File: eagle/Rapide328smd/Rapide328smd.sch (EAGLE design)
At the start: 34 parts, among them IC1 MEGA8-AI, J1 AVR_SPI_PRG_6PTH

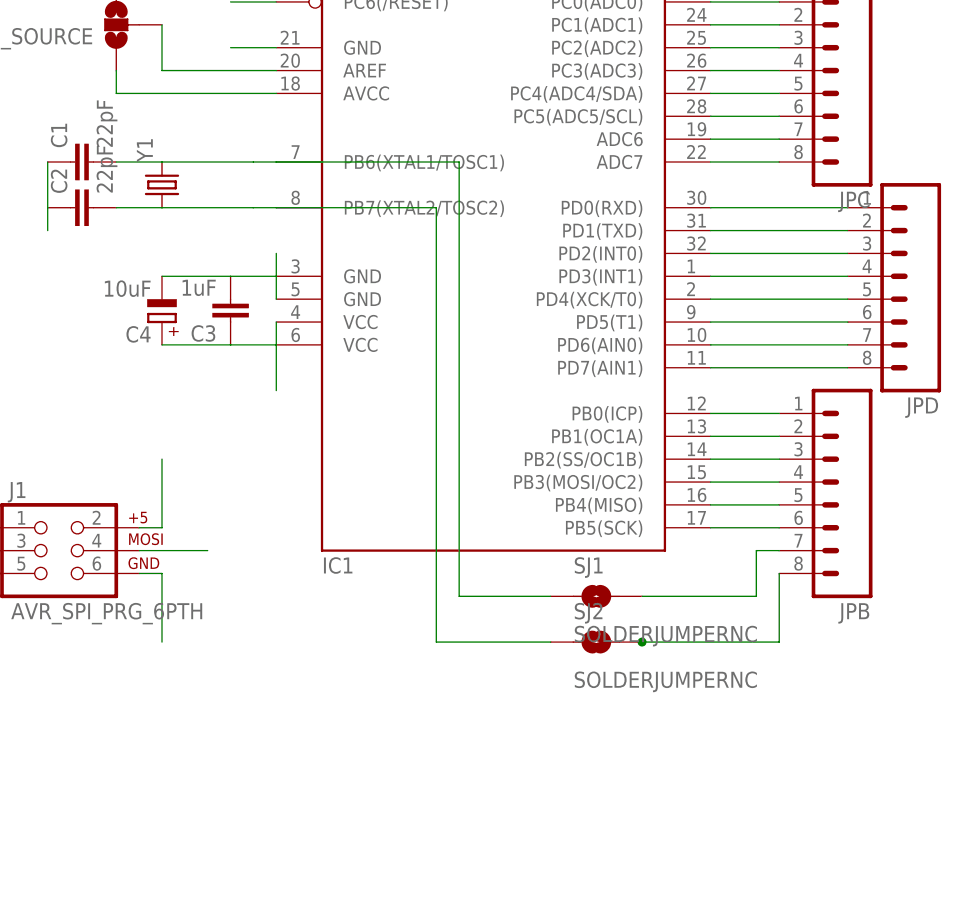
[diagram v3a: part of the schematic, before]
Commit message: Wiring done, now labelling.
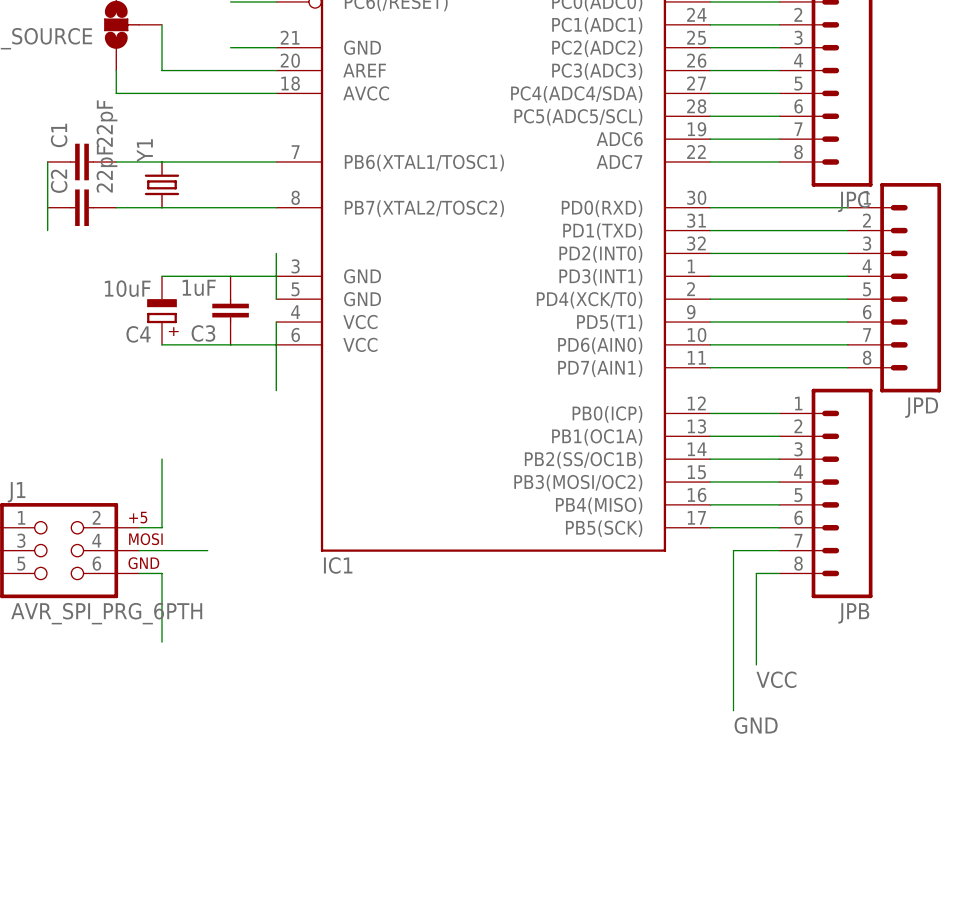
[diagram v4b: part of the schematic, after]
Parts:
- removed SJ1, SJ2: SOLDERJUMPERNC, SparkFun-Passives:SOLDERJUMPERNC
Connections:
- removed net N$23: JPB.7, SJ1.2
- removed net N$24: JPB.8, SJ2.2
- net GND: now also JPB.7
- net N$1: no longer SJ1.1
- net N$26: no longer SJ2.1
- net VCC: now also JPB.8
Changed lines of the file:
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@@
 <part name="JPD" library="SparkFun-Connectors" deviceset="M08" device="1X08"/>
 <part name="JPB" library="SparkFun-Connectors" deviceset="M08" device="1X08"/>
-<part name="SJ1" library="SparkFun-Passives" deviceset="SOLDERJUMPER" device="NC"/>
-<part name="SJ2" library="SparkFun-Passives" deviceset="SOLDERJUMPER" device="NC"/>
 <part name="JP1" library="SparkFun-Connectors" deviceset="M16" device="1X16_NO_SILK"/>
 <part name="JP2" library="SparkFun-Connectors" deviceset="M16" device="1X16_NO_SILK"/>
@@
 <instance part="JPD" gate="G$1" x="101.6" y="53.34" rot="R180"/>
 <instance part="JPB" gate="G$1" x="93.98" y="30.48" rot="R180"/>
-<instance part="SJ1" gate="1" x="68.58" y="17.78"/>
-<instance part="SJ2" gate="1" x="68.58" y="12.7"/>
 <instance part="JP1" gate="G$1" x="137.16" y="63.5"/>
 <instance part="JP2" gate="G$1" x="152.4" y="63.5"/>
@@
 <wire x1="162.56" y1="43.18" x2="162.56" y2="38.1" width="0.1524" layer="91"/>
 </segment>
+<segment>
+<pinref part="JPB" gate="G$1" pin="7"/>
+<wire x1="88.9" y1="22.86" x2="83.82" y2="22.86" width="0.1524" layer="91"/>
+<wire x1="83.82" y1="22.86" x2="83.82" y2="5.08" width="0.1524" layer="91"/>
+<label x="83.82" y="2.54" size="1.778" layer="95"/>
+</segment>
 </net>
 <net name="VCC" class="0">
@@
 <wire x1="147.32" y1="81.28" x2="147.32" y2="86.36" width="0.1524" layer="91"/>
 </segment>
+<segment>
+<pinref part="JPB" gate="G$1" pin="8"/>
+<wire x1="88.9" y1="20.32" x2="86.36" y2="20.32" width="0.1524" layer="91"/>
+<wire x1="86.36" y1="20.32" x2="86.36" y2="10.16" width="0.1524" layer="91"/>
+<label x="86.36" y="7.62" size="1.778" layer="95"/>
+</segment>
 </net>
 <net name="VRAW" class="0">
@@
 <wire x1="15.24" y1="66.04" x2="20.32" y2="66.04" width="0.1524" layer="91"/>
 <pinref part="IC1" gate="G$1" pin="PB6(XTAL1/TOSC1)"/>
-<wire x1="20.32" y1="66.04" x2="30.48" y2="66.04" width="0.1524" layer="91"/>
-<pinref part="SJ1" gate="1" pin="1"/>
-<wire x1="30.48" y1="66.04" x2="33.02" y2="66.04" width="0.1524" layer="91"/>
-<wire x1="63.5" y1="17.78" x2="53.34" y2="17.78" width="0.1524" layer="91"/>
-<wire x1="53.34" y1="17.78" x2="53.34" y2="66.04" width="0.1524" layer="91"/>
-<wire x1="53.34" y1="66.04" x2="33.02" y2="66.04" width="0.1524" layer="91"/>
+<wire x1="20.32" y1="66.04" x2="33.02" y2="66.04" width="0.1524" layer="91"/>
 </segment>
 </net>
@@
 <pinref part="IC1" gate="G$1" pin="PB7(XTAL2/TOSC2)"/>
 <pinref part="Y1" gate="G$1" pin="1"/>
-<wire x1="33.02" y1="60.96" x2="30.48" y2="60.96" width="0.1524" layer="91"/>
 <pinref part="C2" gate="G$1" pin="2"/>
-<wire x1="30.48" y1="60.96" x2="20.32" y2="60.96" width="0.1524" layer="91"/>
+<wire x1="33.02" y1="60.96" x2="20.32" y2="60.96" width="0.1524" layer="91"/>
 <wire x1="20.32" y1="60.96" x2="15.24" y2="60.96" width="0.1524" layer="91"/>
-<pinref part="SJ2" gate="1" pin="1"/>
-<wire x1="63.5" y1="12.7" x2="50.8" y2="12.7" width="0.1524" layer="91"/>
-<wire x1="50.8" y1="12.7" x2="50.8" y2="60.96" width="0.1524" layer="91"/>
-<wire x1="50.8" y1="60.96" x2="33.02" y2="60.96" width="0.1524" layer="91"/>
 </segment>
 </net>
@@
 </segment>
 </net>
-<net name="N$23" class="0">
-<segment>
-<pinref part="SJ1" gate="1" pin="2"/>
-<wire x1="73.66" y1="17.78" x2="86.36" y2="17.78" width="0.1524" layer="91"/>
-<wire x1="86.36" y1="17.78" x2="86.36" y2="22.86" width="0.1524" layer="91"/>
-<pinref part="JPB" gate="G$1" pin="7"/>
-<wire x1="86.36" y1="22.86" x2="88.9" y2="22.86" width="0.1524" layer="91"/>
-</segment>
-</net>
-<net name="N$24" class="0">
-<segment>
-<wire x1="73.66" y1="12.7" x2="88.9" y2="12.7" width="0.1524" layer="91"/>
-<wire x1="88.9" y1="12.7" x2="88.9" y2="20.32" width="0.1524" layer="91"/>
-<pinref part="JPB" gate="G$1" pin="8"/>
-<pinref part="SJ2" gate="1" pin="2"/>
-<junction x="73.66" y="12.7"/>
-</segment>
-</net>

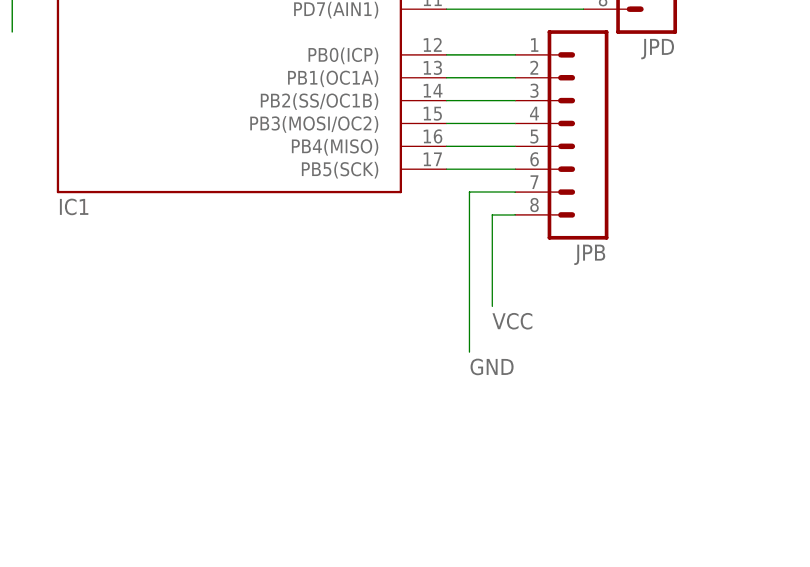
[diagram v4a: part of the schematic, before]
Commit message: Small modifications : added a useable SMD led on PB5 (SCK), added +/- labels on the back of the board, changed a few wire width.
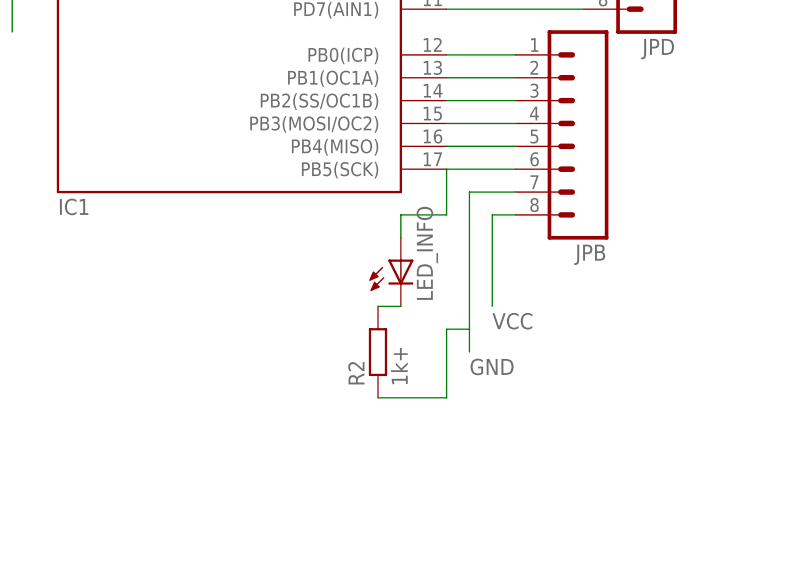
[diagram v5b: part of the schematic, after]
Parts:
- added LED_INFO: (no value), led:LEDKA-3528ASYC
- added R2: 1k+, resistor:R-EU_0204/5
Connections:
- new net N$3: LED_INFO.C, R2.2
- net GND: now also R2.1
- net SCK: now also LED_INFO.A
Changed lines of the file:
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@@
 <part name="JP10" library="SparkFun-Connectors" deviceset="M16" device="1X16_NO_SILK"/>
 <part name="H4" library="holes" deviceset="MOUNT-HOLE" device="2.8"/>
+<part name="R2" library="resistor" deviceset="R-EU_" device="0204/5" value="1k+"/>
+<part name="LED_INFO" library="led" deviceset="LED" device="KA-3528ASYC"/>
 </parts>
 <sheets>
@@
 <instance part="JP10" gate="G$1" x="149.86" y="-45.72"/>
 <instance part="H4" gate="G$1" x="-45.72" y="7.62"/>
+<instance part="R2" gate="G$1" x="73.66" y="5.08" rot="R90"/>
+<instance part="LED_INFO" gate="G$1" x="76.2" y="15.24"/>
 </instances>
 <busses>
@@
 <pinref part="JPB" gate="G$1" pin="7"/>
 <wire x1="88.9" y1="22.86" x2="83.82" y2="22.86" width="0.1524" layer="91"/>
-<wire x1="83.82" y1="22.86" x2="83.82" y2="5.08" width="0.1524" layer="91"/>
+<wire x1="83.82" y1="22.86" x2="83.82" y2="7.62" width="0.1524" layer="91"/>
 <label x="83.82" y="2.54" size="1.778" layer="95"/>
+<pinref part="R2" gate="G$1" pin="1"/>
+<wire x1="83.82" y1="7.62" x2="83.82" y2="5.08" width="0.1524" layer="91"/>
+<wire x1="73.66" y1="0" x2="81.28" y2="0" width="0.1524" layer="91"/>
+<wire x1="81.28" y1="0" x2="81.28" y2="7.62" width="0.1524" layer="91"/>
+<wire x1="81.28" y1="7.62" x2="83.82" y2="7.62" width="0.1524" layer="91"/>
 </segment>
 </net>
@@
 <pinref part="JPB" gate="G$1" pin="6"/>
 <wire x1="81.28" y1="25.4" x2="88.9" y2="25.4" width="0.1524" layer="91"/>
+<wire x1="81.28" y1="25.4" x2="81.28" y2="20.32" width="0.1524" layer="91"/>
+<pinref part="LED_INFO" gate="G$1" pin="A"/>
+<wire x1="81.28" y1="20.32" x2="76.2" y2="20.32" width="0.1524" layer="91"/>
+<wire x1="76.2" y1="20.32" x2="76.2" y2="17.78" width="0.1524" layer="91"/>
 </segment>
 </net>
@@
 </segment>
 </net>
+<net name="N$3" class="0">
+<segment>
+<pinref part="LED_INFO" gate="G$1" pin="C"/>
+<pinref part="R2" gate="G$1" pin="2"/>
+<wire x1="76.2" y1="10.16" x2="73.66" y2="10.16" width="0.1524" layer="91"/>
+</segment>
+</net>
